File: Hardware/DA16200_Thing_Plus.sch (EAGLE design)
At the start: 43 parts, among them J1 SWD, J2 THING_PLUS, J3 Qwiic, J5 USB C, J6 microSD, Q1 20V/4.2A/52mΩ/1.4W, U3 MCP73831, U7 3.3V

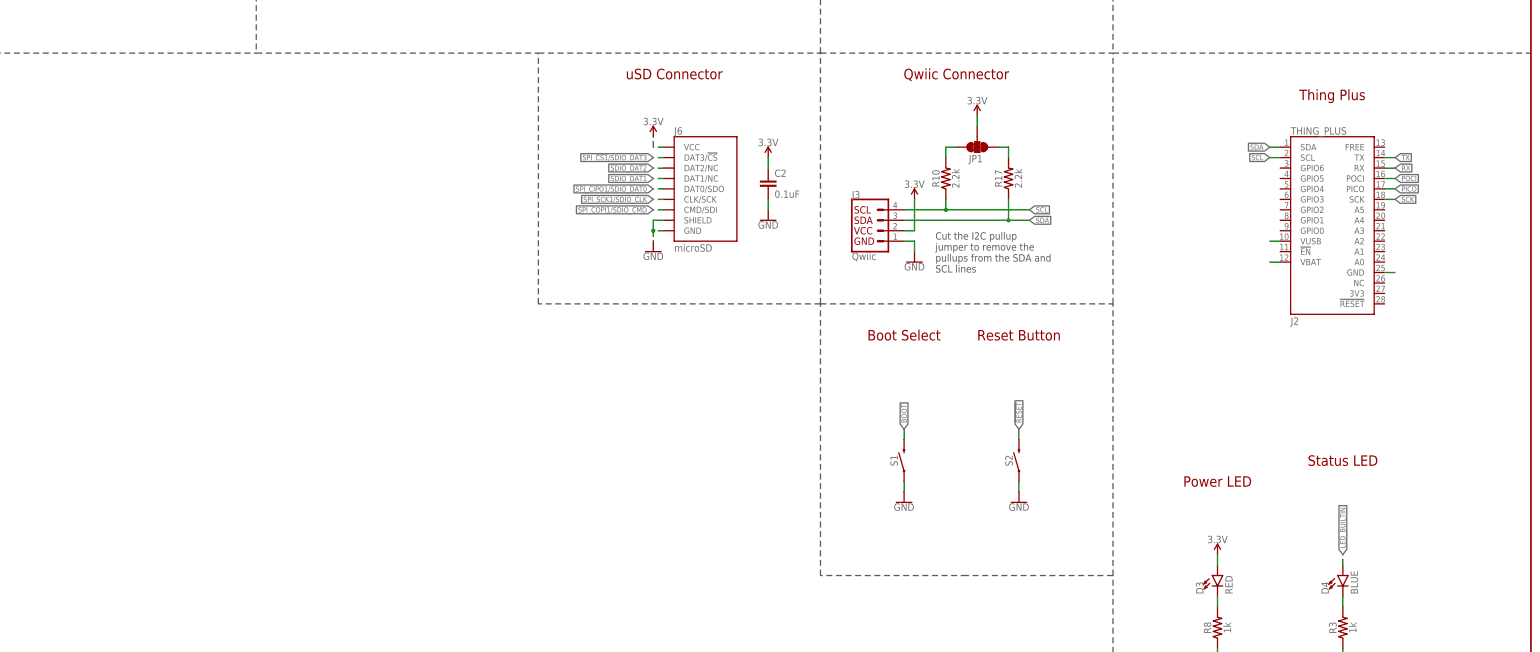
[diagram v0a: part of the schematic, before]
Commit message: Working on initial design
* Schematic almost done
* Laying-out parts
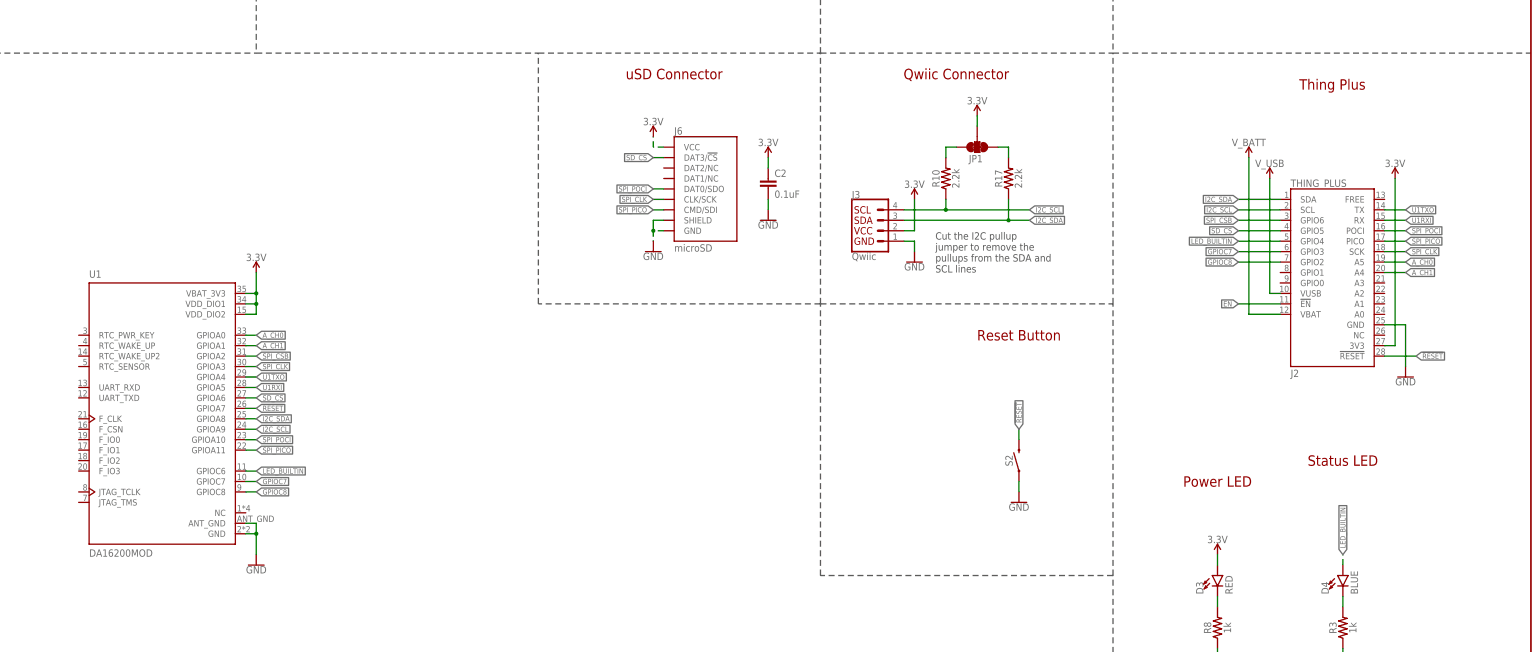
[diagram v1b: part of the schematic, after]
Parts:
- removed S1: MOMENTARY-SWITCH-SPST-SMD-5.2MM-TALL, SparkFun-Switches:MOMENTARY-SWITCH-SPST-SMD-5.2MM-TALL
- added U1: DA16200MOD, SparkFun-RF:DA16200MOD-AAC4WA32
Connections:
- removed net BOOT: S1.2
- removed net N$20: J2.GND
- removed net N$6: J2.VUSB
- removed net N$8: J2.VBAT
- removed net PICO: J2.PICO
- removed net POCI: J2.POCI
- removed net RX: J2.RX
- removed net SCK: J2.SCK
- removed net SCL: J2.SCL, J3.4, R10.1
- removed net SDA: J2.SDA, J3.3, R17.1
- removed net SDIO_DAT1: J6.DAT1/NC
- removed net SDIO_DAT2: J6.DAT2/NC
- removed net SPI_!CS1!/SDIO_DAT3: J6.DAT3/!CS!
- removed net SPI_CIPO1/SDIO_DAT0: J6.DAT0/SDO
- removed net SPI_COPI1/SDIO_CMD: J6.CMD/SDI
- removed net SPI_SCK1/SDIO_CLK: J6.CLK/SCK
- removed net TX: J2.TX
- new net A_CH0: J2.A5, U1.GPIOA0
- new net A_CH1: J2.A4, U1.GPIOA1
- new net GPIOC7: J2.GPIO3, U1.GPIOC7
- new net GPIOC8: J2.GPIO2, U1.GPIOC8
- new net I2C_SCL: J2.SCL, J3.4, R10.1, U1.GPIOA9
- new net I2C_SDA: J2.SDA, J3.3, R17.1, U1.GPIOA8
- new net SD_CS: J2.GPIO5, J6.DAT3/!CS!, U1.GPIOA6
- new net SPI_CLK: J2.SCK, J6.CLK/SCK, U1.GPIOA3
- new net SPI_CSB: J2.GPIO6, U1.GPIOA2
- new net SPI_PICO: J2.PICO, J6.CMD/SDI, U1.GPIOA11
- new net SPI_POCI: J2.POCI, J6.DAT0/SDO, U1.GPIOA10
- new net U1RXI: J2.RX, U1.GPIOA5
- new net U1TXO: J2.TX, U1.GPIOA4
- net !RESET!: now also J2.!RESET, U1.GPIOA7
- net 3.3V: now also J2.3V3, U1.VBAT_3V3, U1.VDD_DIO1, U1.VDD_DIO2
- net EN: now also J2.!EN
- net GND: now also J2.GND, U1.ANT_GND, U1.GND; no longer S1.1
- net LED_BUILTIN: now also J2.GPIO4, U1.GPIOC6
- net V_BATT: now also J2.VBAT
- net V_USB: now also J2.VUSB
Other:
- note removed: "Boot Select"
- moved on the sheet: J2

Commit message: Working on schematic
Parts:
- removed J1: SWD, SparkFun-Connectors:CORTEX_JTAG_DEBUG_MINIMUM_PTH
- removed TP1, TP2, TP3: TEST-POINT3X4, SparkFun-Connectors:TEST-POINT3X4
- added C1: 0.1uF, SparkFun-Capacitors:0.1UF-0603-25V-(+80/-20%)
- added C3: DNP, SparkFun-Capacitors:DNP-0603_NO_CREAM
- added J7: CORTEX_JTAG_DEBUG_PTH_NS, SparkFun-Connectors:CORTEX_JTAG_DEBUG_PTH_NS
- added R5, R7: 4.7k, SparkFun-Resistors:4.7KOHM-0603-1/10W-1%
- added R9: DNP, SparkFun-Resistors:DNP-0603_NO_CREAM
- added U2: CH340E_MSOP10, SparkFun-IC-Comms:CH340E_MSOP10
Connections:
- removed net SWDCK: J1.SWDCLK, TP1.1
- removed net SWDIO: J1.SWDIO, TP2.1
- new net HDR_RTC_WAKE2: C3.1, R5.2, R7.2, U1.RTC_WAKE_UP2
- new net RTC_PWR_KEY: R9.2, U1.RTC_PWR_KEY
- new net RTC_WAKE1: U1.RTC_WAKE_UP
- new net TCLK: J7.SWDCLK/TCK, U1.JTAG_TCLK
- new net TMS: J7.SWDIO/TMS, U1.JTAG_TMS
- new net U0RXI: U1.UART_RXD, U2.TXO
- new net U0TXO: U1.UART_TXD, U2.RXI
- net !RESET!: now also J7.!RESET; no longer J1.!RESET, TP3.1
- net 3.3V: now also C1.1, J7.VCC, R9.1, U2.V3, U2.VCC; no longer J1.VCC
- net GND: now also C1.2, C3.2, J5.SHLD, J7.GND@3, J7.GND@5, J7.GNDDTCT, R5.1, R7.1, U2.GND; no longer J1.GND
- net USB_N: now also U2.UD-
- net USB_P: now also U2.UD+
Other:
- moved on the sheet: C2, D3, D4, J2, J3, J5, J6, JP1, R1, R10, R17, R3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

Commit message: Working on schematic
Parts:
- added JP2: JUMPER-SMT_2_NC_TRACE_SILK, SparkFun-Jumpers:JUMPER-SMT_2_NC_TRACE_SILK
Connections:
- new net N$4: D3.A, JP2.1
- net 3.3V: now also JP2.2; no longer D3.A
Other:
- note added: "DA16200 Module"
- note added: "USB-C Firmware Upload"
- note removed: "USB Connector"
- moved on the sheet: C1, C2, D3, D4, J2, J3, J5, J6, J7, JP1, R1, R10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

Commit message: Pete's schematic suggestions
* Add jumper to disable PWR LED
* TVS protection for D+/D- lines
* Add low value resistor (200) on reset line
* multiple charge current options
* Add 100 ohm between gate of Q2 and V_USB
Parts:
- added D5: PRTR5V0U2F, SparkFun-IC-Power:PRTR5V0U2F
- added JP3: JUMPER-SMT_3_1-NC_TRACE_SILK, SparkFun-Jumpers:JUMPER-SMT_3_1-NC_TRACE_SILK
- added R11, R12: 27, SparkFun-Resistors:27OHM-0603-1/10W-1%
- added R13: 200, SparkFun-Resistors:200OHM-0603-1/10W-1%
- added R14: 10k, SparkFun-Resistors:10KOHM-0603-1/10W-1%
- added R18: 100, SparkFun-Resistors:100OHM-0603-1/10W-1%
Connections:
- removed net USB_N: J5.D-, U2.UD-
- removed net USB_P: J5.D+, U2.UD+
- new net N$10: JP3.3, R6.2
- new net N$13: D5.6, R11.1
- new net N$16: D5.4, R12.1
- new net N$18: R11.2, U2.UD+
- new net N$19: R12.2, U2.UD-
- new net N$20: JP3.1, R14.2
- new net N$21: Q1.G, R18.2
- new net N$5: D5.1, J5.D+
- new net N$6: D5.3, J5.D-
- new net N$8: R13.1, S2.2
- net !RESET!: now also R13.2; no longer J7.!RESET, S2.2
- net GND: now also D5.2, R14.1
- net N$14: now also JP3.2; no longer R6.2
- net V_USB: now also D5.5, R18.1; no longer Q1.G
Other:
- note added: "Charge current: I_CHG = 1000 / R_PROG R_PROG=2k : I_CHG=500mA R_PROG=10k: I_CHG=100mA"
- note removed: "Charge current: I_CHG = 1000 / R_PROG R_PROG=2k : I_CHG=500mA"
- moved on the sheet: C1, C10, J4, J5, R1, R15, R4, R6, S2, U2

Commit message: Switch pins around
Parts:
- removed H1, H2: STAND-OFF, SparkFun-Hardware:STAND-OFF
- added JP4: JUMPER-SMT_2_NO_SILK, SparkFun-Jumpers:JUMPER-SMT_2_NO_SILK
- C1: device SparkFun-Capacitors:0.1UF-0603-25V-(+80/-20%) -> SparkFun-Capacitors:0.1UF-0402T-16V-10%
- C3: device SparkFun-Capacitors:DNP-0603_NO_CREAM -> SparkFun-Capacitors:DNP-0402-TIGHT
- R11, R12: value 27 -> 27OHM; device SparkFun-Resistors:27OHM-0603-1/10W-1% -> SparkFun-Resistors:27OHM
- R13: value 200 -> 200OHM-0402T-1/16W-1%; device SparkFun-Resistors:200OHM-0603-1/10W-1% -> SparkFun-Resistors:200OHM-0402T-1/16W-1%
- R14: device SparkFun-Resistors:10KOHM-0603-1/10W-1% -> SparkFun-Resistors:10KOHM-0402T-1/16W-1%
- R18: device SparkFun-Resistors:100OHM-0603-1/10W-1% -> SparkFun-Resistors:100OHM-0402-TIGHT-1/16W-1%
- R5, R7: device SparkFun-Resistors:4.7KOHM-0603-1/10W-1% -> SparkFun-Resistors:4.7KOHM-0402T-1/16W-1%
- R6: value 2.0k -> 2.0K; device SparkFun-Resistors:2.0KOHM-0603-1/10W-5% -> SparkFun-Resistors:2.0KOHM-0402T-1/16W-1%
- R9: device SparkFun-Resistors:DNP-0603_NO_CREAM -> SparkFun-Resistors:DNP-0402T
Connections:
- removed net !RESET!: J2.!RESET, R13.2, U1.GPIOA7
- removed net A_CH0: J2.A5, U1.GPIOA0
- removed net A_CH1: J2.A4, U1.GPIOA1
- removed net LED_BUILTIN: D4.A, J2.GPIO4, U1.GPIOC6
- removed net SPI_CLK: J2.SCK, J6.CLK/SCK, U1.GPIOA3
- new net !RESET!/SPI_CLK: J2.!RESET, J2.SCK, J6.CLK/SCK, R13.2, U1.GPIOA7
- new net A_CH2: J2.A5, U1.GPIOA2
- new net A_CH3: J2.A4, U1.GPIOA3
- new net GPIOC6: J2.GPIO0, J7.!RESET, U1.GPIOC6
- new net N$24: J5.SHLD, JP4.2
- new net RTC_WAKE2: J2.GPIO1
- new net STAT_LED: D4.A, J2.GPIO4, U1.GPIOA11
- net GND: now also JP4.1; no longer J5.SHLD
- net GPIOC7: now also J7.SWO/TDO; no longer J2.GPIO3
- net GPIOC8: now also J7.NC/TDI; no longer J2.GPIO2
- net I2C_SCL: now also U1.GPIOA1; no longer U1.GPIOA9
- net I2C_SDA: now also U1.GPIOA0; no longer U1.GPIOA8
- net RTC_PWR_KEY: now also J2.GPIO3
- net RTC_WAKE1: now also J2.GPIO2
- net SD_CS: now also U1.GPIOA10; no longer U1.GPIOA6
- net SPI_CSB: now also U1.GPIOA6; no longer U1.GPIOA2
- net SPI_PICO: now also U1.GPIOA8; no longer U1.GPIOA11
- net SPI_POCI: now also U1.GPIOA9; no longer U1.GPIOA10
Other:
- note added: "!RESET!/CLK"
- note added: "A_CH2"
- note added: "A_CH3"
- note added: "CSB"
- note added: "PICO"
- note added: "POCI"
- note added: "SCL"
- note added: "SDA"
- note added: "SD_CS"
- note added: "STAT_LED"
- moved on the sheet: R1, R4

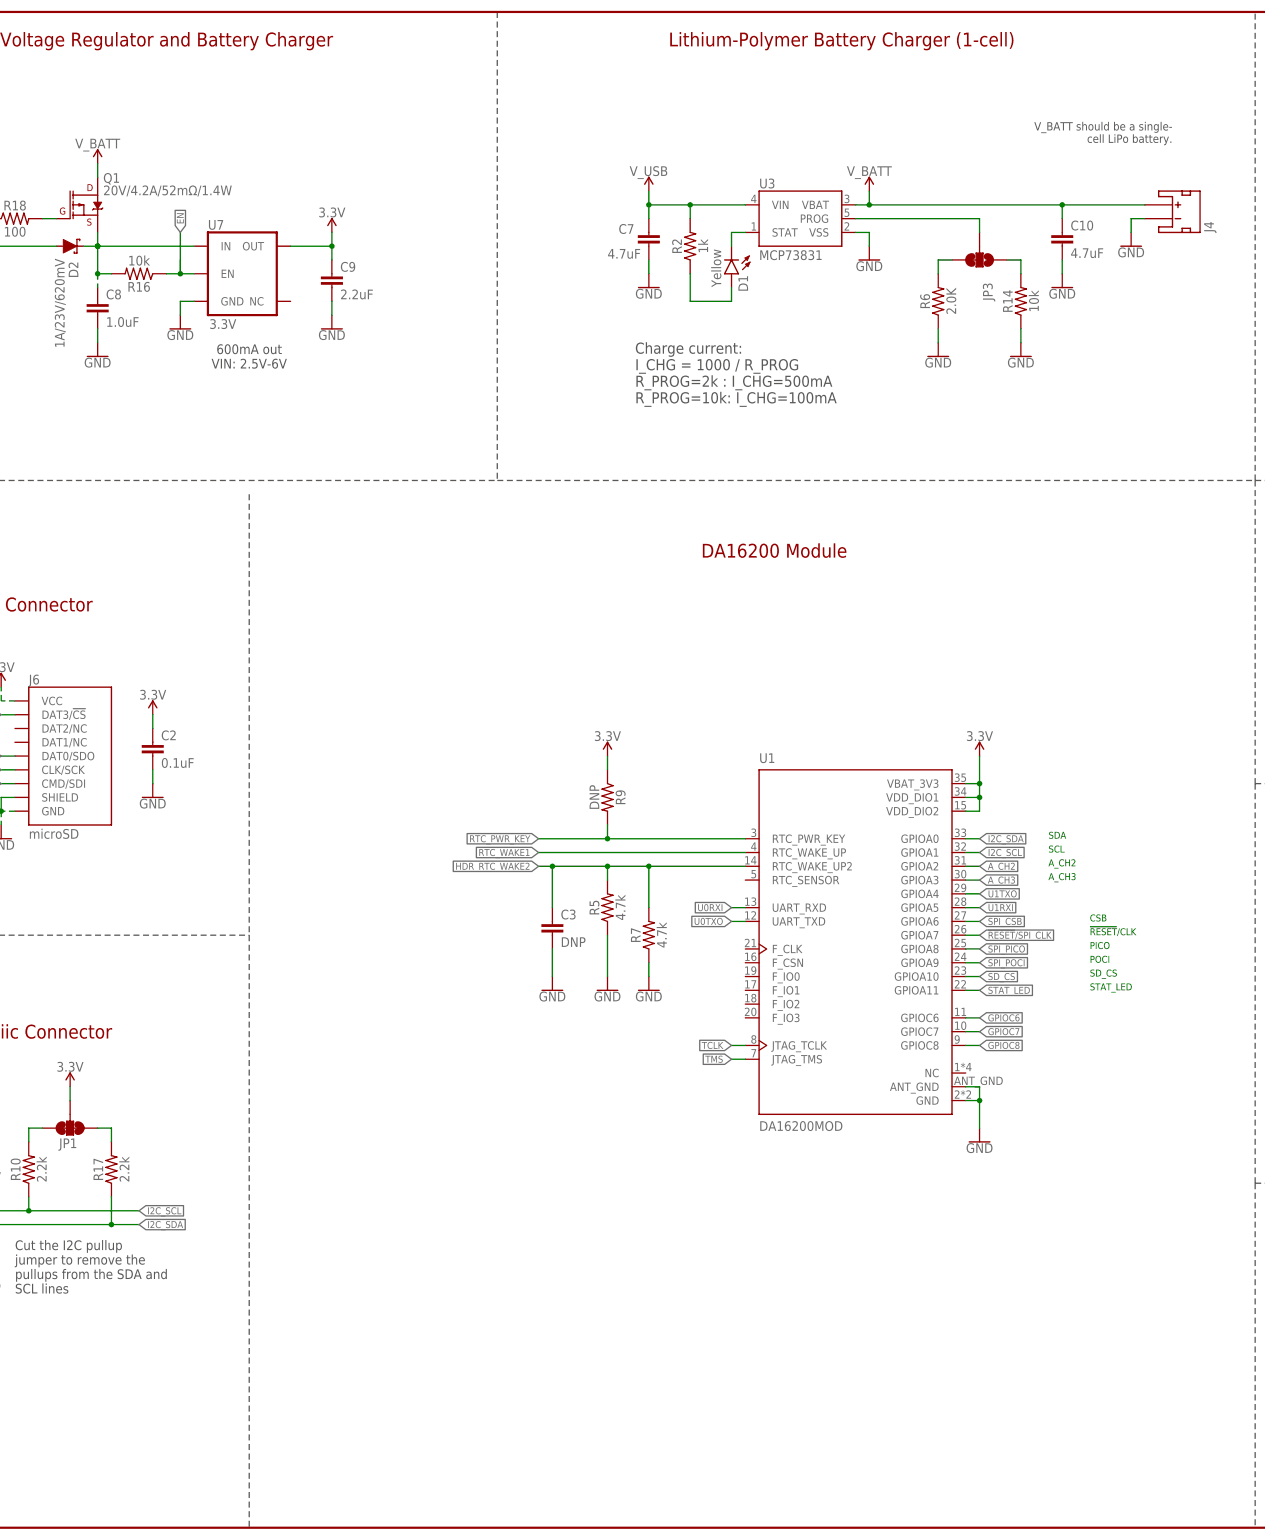
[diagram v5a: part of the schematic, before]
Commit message: Eric's suggestions
* Add external flash
* Add a jumper to measure current draw
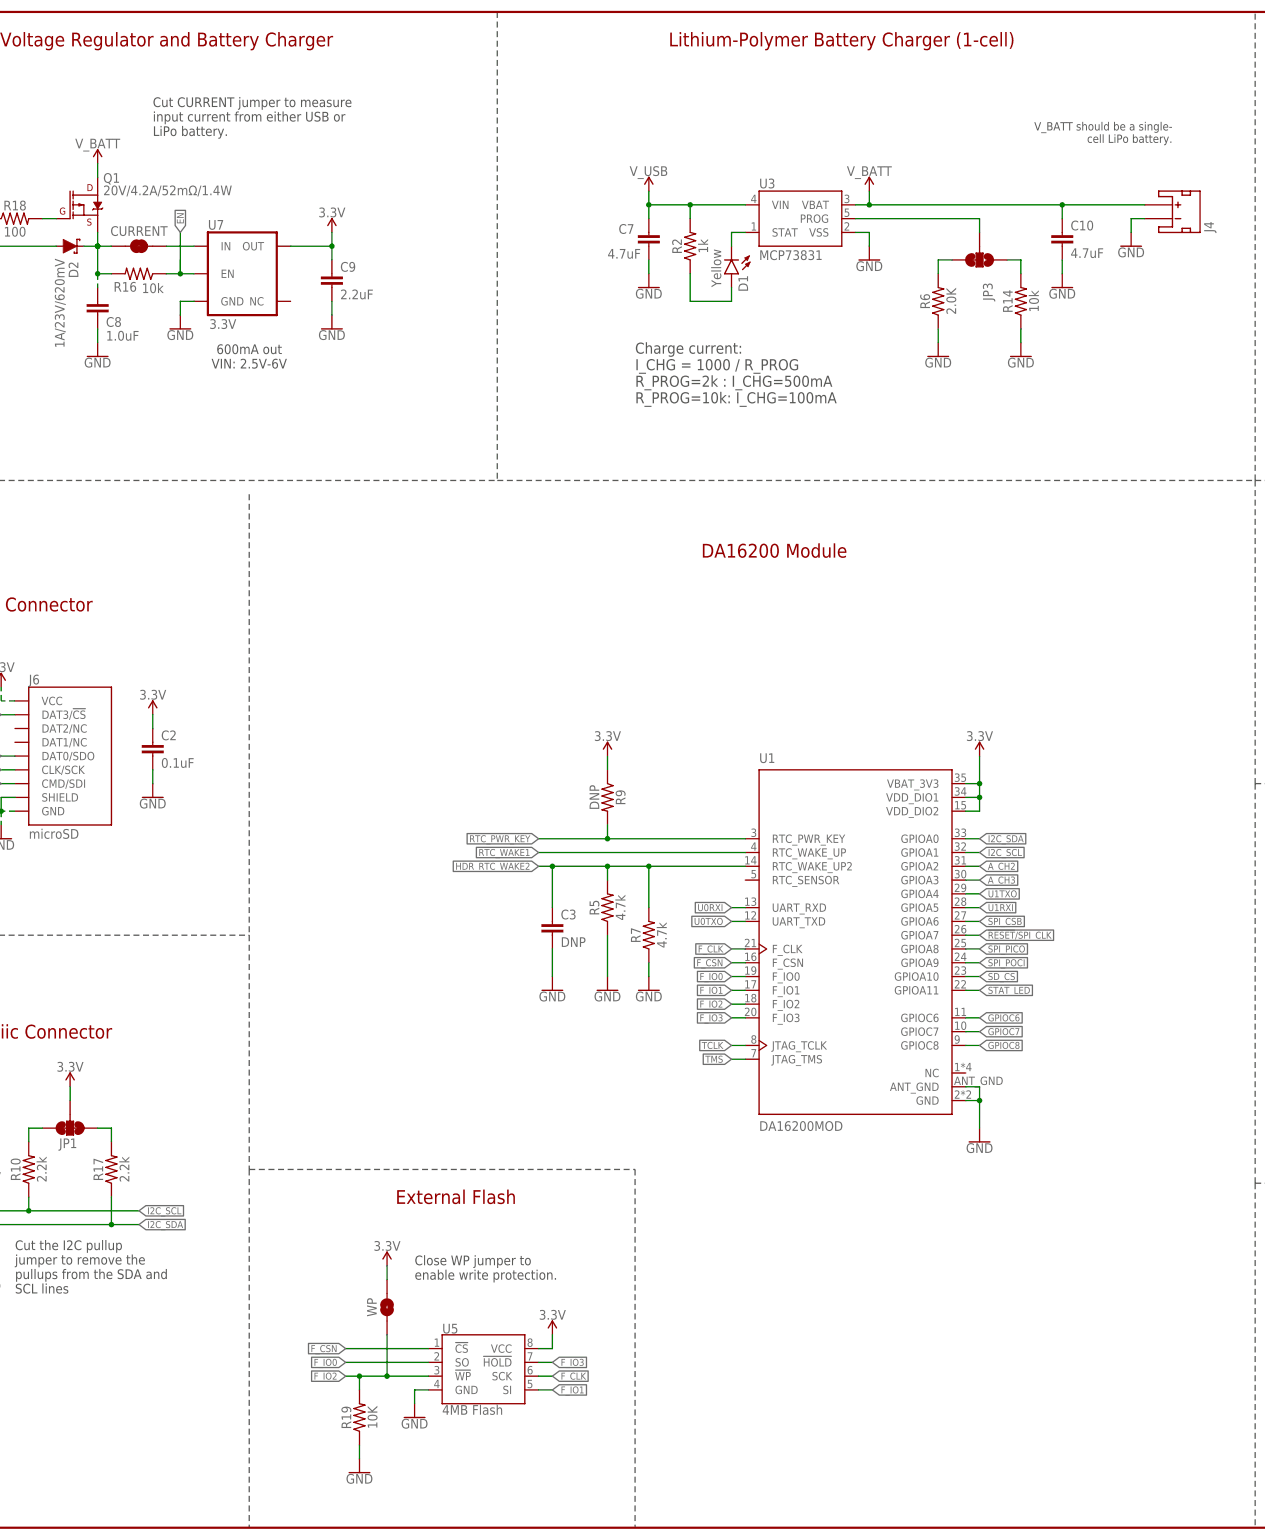
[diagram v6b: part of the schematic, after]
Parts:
- added CURRENT: JUMPER-COMBO_2_NC_TRACE, SparkFun-Jumpers:JUMPER-COMBO_2_NC_TRACE
- added R19: 10K, SparkFun-Resistors:10KOHM-0402-1/10W-0.1%
- added U5: 4MB Flash, SparkFun-IC-Memory:AT25SF041
- added WP: JUMPER-SMT_2_NO_SILK, SparkFun-Jumpers:JUMPER-SMT_2_NO_SILK
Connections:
- new net F_CLK: U1.F_CLK, U5.SCK
- new net F_CSN: U1.F_CSN, U5.!CS
- new net F_IO0: U1.F_IO0, U5.SO
- new net F_IO1: U1.F_IO1, U5.SI
- new net F_IO2: R19.2, U1.F_IO2, U5.!WP, WP.1
- new net F_IO3: U1.F_IO3, U5.!HOLD
- new net N$22: CURRENT.2, U7.IN
- net 3.3V: now also U5.VCC, WP.2
- net GND: now also R19.1, U5.GND
- net N$15: now also CURRENT.1; no longer U7.IN
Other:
- note added: "Close WP jumper to enable write protection."
- note added: "Cut CURRENT jumper to measure input current from either USB or LiPo battery."
- note added: "External Flash"
- note removed: "!RESET!/CLK"
- note removed: "A_CH2"
- note removed: "A_CH3"
- note removed: "CSB"
- note removed: "PICO"
- note removed: "POCI"
- note removed: "SCL"
- note removed: "SDA"
- note removed: "SD_CS"
- note removed: "STAT_LED"

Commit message: Routing
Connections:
- removed net RTC_WAKE2: J2.GPIO1
- net HDR_RTC_WAKE2: now also J2.GPIO1
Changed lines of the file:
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@@
 <label x="129.54" y="121.92" size="1.27" layer="95" rot="R180" xref="yes"/>
+</segment>
+<segment>
+<pinref part="J2" gate="G$1" pin="GPIO1"/>
+<wire x1="373.38" y1="111.76" x2="363.22" y2="111.76" width="0.1524" layer="91"/>
+<label x="363.22" y="111.76" size="1.27" layer="95" rot="R180" xref="yes"/>
 </segment>
 </net>
@@
 </segment>
 </net>
-<net name="RTC_WAKE2" class="0">
-<segment>
-<pinref part="J2" gate="G$1" pin="GPIO1"/>
-<wire x1="373.38" y1="111.76" x2="363.22" y2="111.76" width="0.1524" layer="91"/>
-<label x="363.22" y="111.76" size="1.27" layer="95" rot="R180" xref="yes"/>
-</segment>
-</net>
